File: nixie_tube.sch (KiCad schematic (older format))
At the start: 24 parts, among them J1 Conn_01x06_Male, J11 dc003a, J2 Conn_01x06_Female, J3 Conn_01x01_Male, J4 Conn_01x01_Female, Q1 SS8550, Q2 FQD5N60C, Q3 Q_NPN_BCE, Q4 TP0610T, U1 MC34063

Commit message: fixed pin position for ss8500
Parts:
- removed Q1: SS8550, TO_SOT_Packages_SMD:SOT-23, symbol MPSA92
- added Q?: Q_PNP_BEC, TO_SOT_Packages_SMD:SOT-23, symbol Q_PNP_BEC
- Q4: value TP0610T -> AO3407
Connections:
- net GND: now also Q?.3 (C)
- net at D1.1 (K), Q2.1 (G): now also Q?.2 (E)
- net at D1.2 (A), R1.1, U1.2: now also Q?.1 (B)
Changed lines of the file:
@@
-$EndComp
-$Comp
-L MPSA92 Q1
-U 1 1 59D515D9
-P 4200 3350
-F 0 "Q1" H 4400 3425 50  0000 L CNN
-F 1 "SS8550" H 4400 3350 50  0000 L CNN
-F 2 "TO_SOT_Packages_SMD:SOT-23" H 4400 3275 50  0000 L CIN
-F 3 "" H 4200 3350 50  0000 L CNN
-	1    4200 3350
-	1    0    0    1
 $EndComp
 $Comp
@@
 P 1825 2300
 F 0 "Q4" H 2025 2375 50  0000 L CNN
-F 1 "TP0610T" H 2025 2300 50  0000 L CNN
+F 1 "AO3407" H 2025 2300 50  0000 L CNN
 F 2 "nixie-tube-fp:SOT-23-alt_solder_on2_3" H 2025 2225 50  0001 L CIN
 F 3 "" H 1825 2300 50  0001 L CNN
@@
 	0    1    -1   0
 $EndComp
+$Comp
+L Q_PNP_BEC Q?
+U 1 1 5A0CBD94
+P 4200 3350
+F 0 "Q?" H 4400 3400 50  0000 L CNN
+F 1 "Q_PNP_BEC" H 4400 3300 50  0000 L CNN
+F 2 "TO_SOT_Packages_SMD:SOT-23" H 4400 3450 50  0001 C CNN
+F 3 "" H 4200 3350 50  0001 C CNN
+	1    4200 3350
+	1    0    0    1
+$EndComp
 $EndSCHEMATC

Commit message: fixed npn pin numbering not same with real device
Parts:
- removed Q3: Q_NPN_BCE, TO_SOT_Packages_SMD:SOT-23, symbol Q_NPN_BCE
- added Q?: MMBTA42LT1, TO_SOT_Packages_SMD:SOT-23, symbol Q_NPN_BEC
- Q1: renamed from Q?; value Q_PNP_BEC -> SS8550
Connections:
- net GND: now also Q?.2 (E)
- net at Q4.1 (G), R5.2: now also Q?.3 (C)
- net at R4.1: now also Q?.1 (B)
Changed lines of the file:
@@
-$EndComp
-$Comp
-L Q_NPN_BCE Q3
-U 1 1 59E61059
-P 1725 2900
-F 0 "Q3" H 1925 2950 50  0000 L CNN
-F 1 "Q_NPN_BCE" H 1925 2850 50  0000 L CNN
-F 2 "TO_SOT_Packages_SMD:SOT-23" H 1925 3000 50  0001 C CNN
-F 3 "" H 1725 2900 50  0001 C CNN
-	1    1725 2900
-	1    0    0    -1
 $EndComp
 $Comp
@@
 $EndComp
 $Comp
-L Q_PNP_BEC Q?
+L Q_PNP_BEC Q1
 U 1 1 5A0CBD94
 P 4200 3350
-F 0 "Q?" H 4400 3400 50  0000 L CNN
-F 1 "Q_PNP_BEC" H 4400 3300 50  0000 L CNN
+F 0 "Q1" H 4400 3400 50  0000 L CNN
+F 1 "SS8550 " H 4400 3300 50  0000 L CNN
 F 2 "TO_SOT_Packages_SMD:SOT-23" H 4400 3450 50  0001 C CNN
 F 3 "" H 4200 3350 50  0001 C CNN
@@
 	1    0    0    1
 $EndComp
+$Comp
+L Q_NPN_BEC Q?
+U 1 1 5A0CE5DA
+P 1725 2900
+F 0 "Q?" H 1925 2950 50  0000 L CNN
+F 1 "MMBTA42LT1" H 1925 2850 50  0000 L CNN
+F 2 "TO_SOT_Packages_SMD:SOT-23" H 1925 3000 50  0001 C CNN
+F 3 "" H 1725 2900 50  0001 C CNN
+	1    1725 2900
+	1    0    0    -1
+$EndComp
 $EndSCHEMATC

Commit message: finalized everything
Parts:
- gave numbers to parts that had none: 1
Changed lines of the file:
@@
 $EndComp
 $Comp
-L Q_NPN_BEC Q?
+L Q_NPN_BEC Q3
 U 1 1 5A0CE5DA
 P 1725 2900
-F 0 "Q?" H 1925 2950 50  0000 L CNN
+F 0 "Q3" H 1925 2950 50  0000 L CNN
 F 1 "MMBTA42LT1" H 1925 2850 50  0000 L CNN
 F 2 "TO_SOT_Packages_SMD:SOT-23" H 1925 3000 50  0001 C CNN

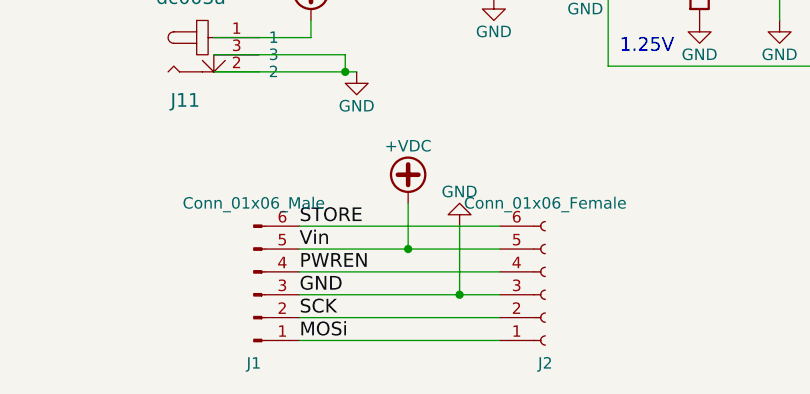
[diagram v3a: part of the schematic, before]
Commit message: fixed correct footprint for pin headers and socket, removed silk screen
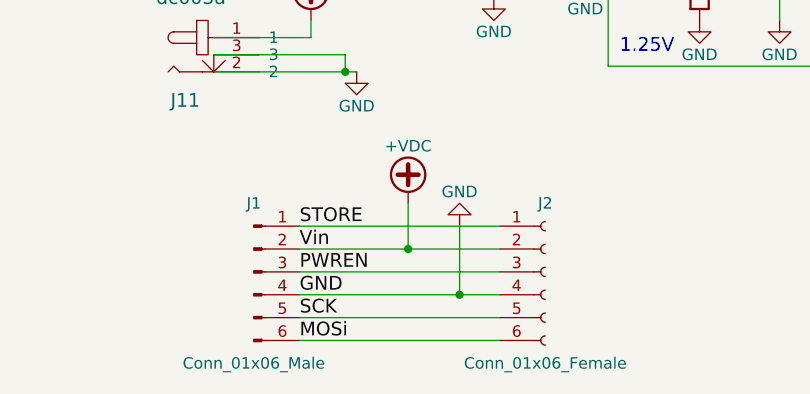
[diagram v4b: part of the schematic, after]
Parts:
- J1: footprint Pin_Headers:Pin_Header_Angled_1x06_Pitch2.54mm -> nixie-tube-fp:Socket_Strip_Angled_1x06_Pitch2.54mm_without_slikscreen
- J2: footprint Socket_Strips:Socket_Strip_Angled_1x06_Pitch2.54mm -> Pin_Headers:Pin_Header_Angled_1x06_Pitch2.54mm
- J4: footprint Socket_Strips:Socket_Strip_Angled_1x01_Pitch2.54mm -> nixie-tube-fp:Socket_Strip_Angled_1x01_Pitch2.54mm_without_silkScreen
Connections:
- net +VDC: now also J1.2 (Pin_2), J2.2 (Pin_2); no longer J1.5 (Pin_5), J2.5 (Pin_5)
- net GND: now also J1.4 (Pin_4), J2.4 (Pin_4); no longer J1.3 (Pin_3), J2.3 (Pin_3)
- net MOSi: now also J1.6 (Pin_6), J2.6 (Pin_6); no longer J1.1 (Pin_1), J2.1 (Pin_1)
- net PWREN: now also J1.3 (Pin_3), J2.3 (Pin_3); no longer J1.4 (Pin_4), J2.4 (Pin_4)
- net SCK: now also J1.5 (Pin_5), J2.5 (Pin_5); no longer J1.2 (Pin_2), J2.2 (Pin_2)
- net STORE: now also J1.1 (Pin_1), J2.1 (Pin_1); no longer J1.6 (Pin_6), J2.6 (Pin_6)
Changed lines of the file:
@@
 F 0 "J4" H 7500 2425 50  0000 C CNN
 F 1 "Conn_01x01_Female" H 7500 2225 50  0000 C CNN
-F 2 "Socket_Strips:Socket_Strip_Angled_1x01_Pitch2.54mm" H 7500 2325 50  0001 C CNN
+F 2 "nixie-tube-fp:Socket_Strip_Angled_1x01_Pitch2.54mm_without_silkScreen" H 7500 2325 50  0001 C CNN
 F 3 "" H 7500 2325 50  0001 C CNN
 	1    7500 2325
@@
 L Conn_01x06_Male J1
 U 1 1 59F6FE01
-P 2000 4900
-F 0 "J1" H 2000 5200 50  0000 C CNN
-F 1 "Conn_01x06_Male" H 2000 4500 50  0000 C CNN
-F 2 "Pin_Headers:Pin_Header_Angled_1x06_Pitch2.54mm" H 2000 4900 50  0001 C CNN
-F 3 "" H 2000 4900 50  0001 C CNN
-	1    2000 4900
-	1    0    0    1
+P 2000 4800
+F 0 "J1" H 2000 5100 50  0000 C CNN
+F 1 "Conn_01x06_Male" H 2000 4400 50  0000 C CNN
+F 2 "nixie-tube-fp:Socket_Strip_Angled_1x06_Pitch2.54mm_without_slikscreen" H 2000 4800 50  0001 C CNN
+F 3 "" H 2000 4800 50  0001 C CNN
+	1    2000 4800
+	1    0    0    -1
 $EndComp
 $Comp
 L Conn_01x06_Female J2
 U 1 1 59F70E4E
-P 3275 4900
-F 0 "J2" H 3275 5200 50  0000 C CNN
-F 1 "Conn_01x06_Female" H 3275 4500 50  0000 C CNN
-F 2 "Socket_Strips:Socket_Strip_Angled_1x06_Pitch2.54mm" H 3275 4900 50  0001 C CNN
-F 3 "" H 3275 4900 50  0001 C CNN
-	1    3275 4900
-	1    0    0    1
+P 3275 4800
+F 0 "J2" H 3275 5100 50  0000 C CNN
+F 1 "Conn_01x06_Female" H 3275 4400 50  0000 C CNN
+F 2 "Pin_Headers:Pin_Header_Angled_1x06_Pitch2.54mm" H 3275 4800 50  0001 C CNN
+F 3 "" H 3275 4800 50  0001 C CNN
+	1    3275 4800
+	1    0    0    -1
 $EndComp
 Text Label 2200 4600 0    60   ~ 0

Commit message: checked all components, modifed some tracks
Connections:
- net MOSi renamed MOSI
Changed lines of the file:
@@
 SCK
 Text Label 2200 5100 0    60   ~ 0
-MOSi
+MOSI
 $Comp
 L GND #PWR011
